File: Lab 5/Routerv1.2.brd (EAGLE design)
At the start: 100 x 80 mm, 48 parts, among them J1 FTDI_DEVICERA_SMT, M1 WIRELESS-NRF24L01, U1 3.3V, U2 GY-521MPU6050

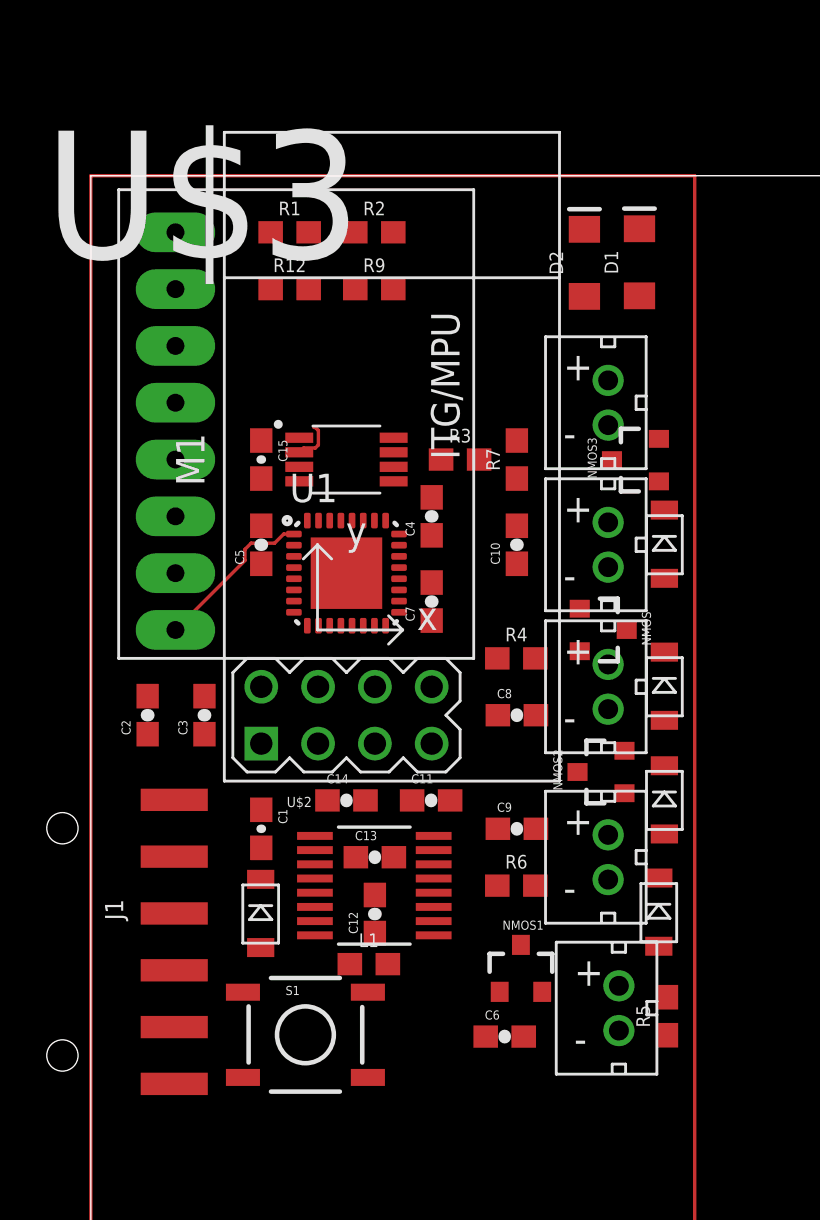
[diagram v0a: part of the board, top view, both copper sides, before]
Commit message: Check routev2.3.brd for one with no error
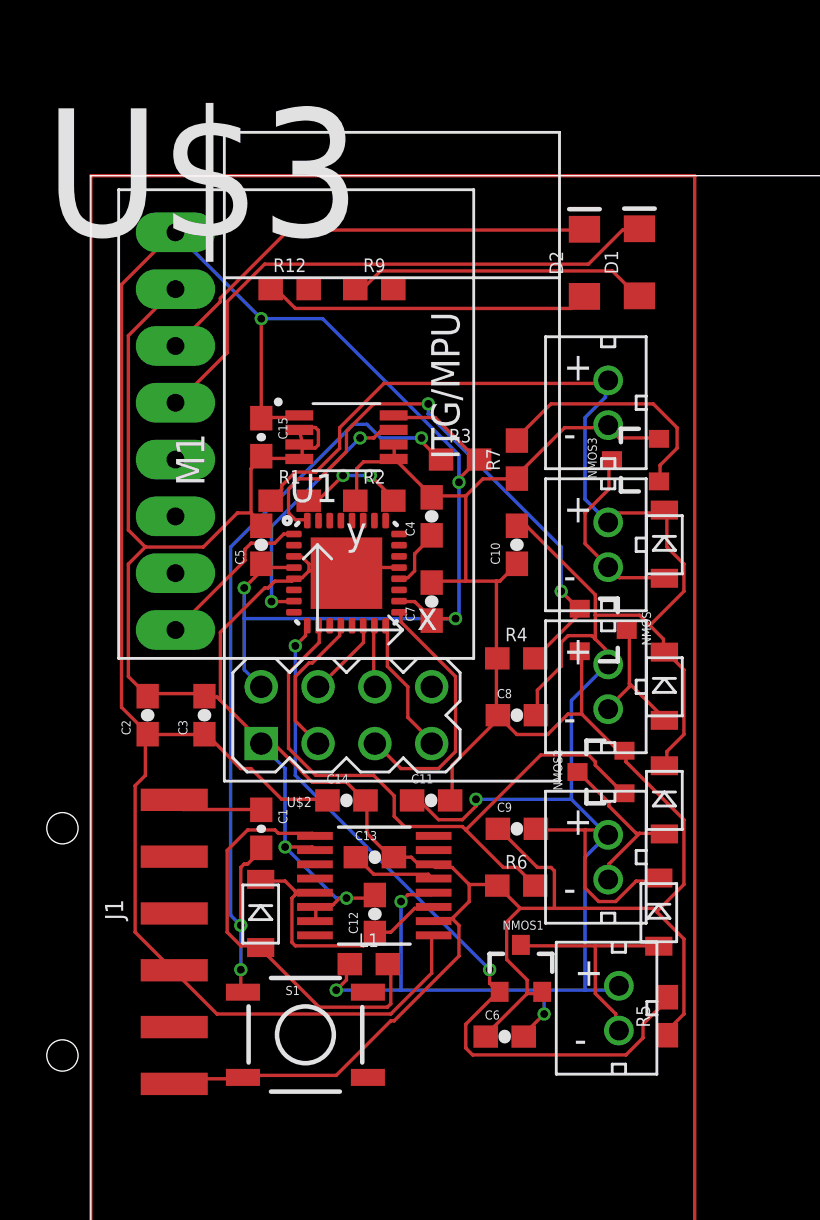
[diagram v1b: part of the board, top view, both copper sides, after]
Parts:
- moved R1 12.0 mm to (8.89, 65.5)
- moved R2 12.0 mm to (12.7, 65.5)
- moved C15 1.00 mm to (7.62, 68.3)
- moved U$3 1.00 mm to (11.4, 68.3)
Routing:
- net GND: track 1.90 -> 183.7 mm, vias 0 -> 2
- net VCC: track 0.00 -> 116.3 mm, vias 0 -> 4
- net BATTERY+: track 0.00 -> 114.2 mm, vias 0 -> 4
- net RESET: track 0.00 -> 36.5 mm, vias 0 -> 3
- net MOTOR2: track 0.00 -> 34.2 mm, vias 0 -> 2
- net MOTOR3: track 0.00 -> 29.4 mm
- net MOTOR1: track 0.00 -> 25.5 mm, vias 0 -> 2
- net IMU-SDA: track 0.00 -> 25.3 mm
- net IMU-SCL: track 0.00 -> 20.5 mm
- net N$1: track 0.00 -> 18.7 mm
- net N$9: track 0.00 -> 14.6 mm
- net N$8: track 0.00 -> 13.5 mm
- net VR-PS: track 0.00 -> 12.2 mm
- net RF-SCK: track 0.00 -> 11.6 mm
- net OSC1: track 0.00 -> 11.6 mm, vias 0 -> 2
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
